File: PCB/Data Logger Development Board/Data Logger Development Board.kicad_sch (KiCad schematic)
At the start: 15 parts, among them J1 TFBS4711-TR1, U1 STM32C091FCP6, U2 TPS631000DRLR, U3 MCP2122T-E/SN

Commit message: Added ADC for reading battery voltage, added temp sensor, added GPS breakout board
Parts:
- removed C2: 22uF, symbol Device:C
- added C10, C7: 100nF, symbol Device:C
- added C8, C9: 20pF, symbol Device:C
- added Q1, Q2, Q3, Q4, Q5, Q6: 2N7002, Package_TO_SOT_SMD:SOT-23_Handsoldering, symbol Transistor_FET:2N7002
- added R10, R11, R13, R15, R18, R20: 1kR, symbol Device:R
- added R12, R14, R16, R17, R19, R5, R6: 100kR, symbol Device:R
- added R7: 15kR, symbol Device:R
- added R8, R9: 10kR, symbol Device:R
- added TH1: NTCG164BH103JT1, symbol Device:Thermistor
- added U4: M95P32-IXMNT/E, SO8N_4X5X1P27_STM, symbol M95P32-IXMNT/E:M95P32-IXMNT_E
- added U5: MCP7940N-I/MS, MSOP8_MC_MCH, symbol MCP7940N-I/MS:MCP7940N-I_MS
- added U6: 120591-1, CONN3_120591-1_TEC, symbol MP000357:120591-1
- added U7: VEML7700-TR, VEML7700-TR, symbol VEML7700-TR:VEML7700-TR
- added U8: ~, symbol M95P32-IXMNT/E:GY-NEO6MV2
- added Y1: 32.768kHz, symbol Device:Crystal
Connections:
- net 3.3V_REG: now also C10.2, C7.1, R6.2, TH1.1, U4.8 (VCC), U5.8 (VCC), U7.2 (VDD), U8.1 (VCC)
- net BAT_OUT: now also R8.1
- net GND: now also C10.1, C7.2, C8.2, C9.2, Q1.2 (S), Q2.2 (S), Q3.2 (S), Q4.2 (S), Q5.2 (S), Q6.2 (S), R12.1, R14.1, R16.1, R17.1, R19.1, R5.1, U4.1 (*S), U6.3 (GND), U8.4 (GND); no longer U3.4 (VSS)
- net I2C_SCL: now also U5.6 (SCL), U7.1 (SCL)
- net I2C_SDA: now also U5.5 (SDA), U7.4 (SDA)
- net MEMORY #WP: now also U4.3 (*W-DQ2)
- net SPI MOSI: now also U4.5 (D-DQ0)
- net SPI_CLK: now also U4.6 (C)
- net SPI_MISO: now also U1.16 (PA11[PA9]), U4.2 (Q-DQ1); no longer U1.13 (PA6)
- net USART1_TX: now also U1.2 (PC14-OSCX_IN); no longer U1.7 (PA0)
- net USART2_RX: now reaches U1.18 (PA13)
- net USART2_RX: now also U8.3 (TX)
- net USART2_TX: now reaches U1.19 (PA14-BOOT0/PA15)
- net USART2_TX: now also U8.2 (RX)
- net MEMORY CS renamed WAKEUP
- net WAKEUP: now also R10.1, R11.2, R13.1, R15.1, R18.1, R20.1
- new net: C9.1, U5.2 (X2), Y1.2
- new net: Q1.1 (G), R11.1, R5.2
- new net: Q1.3 (D), R9.2
- new net: U5.3 (VBAT), U6.1 (VBat), U6.2 (VBat)
- new net: Q6.1 (G), R19.2, R20.2
- new net: Q3.1 (G), R13.2, R14.2
- new net: Q6.3 (D), U3.4 (VSS)
- new net: Q5.1 (G), R17.2, R18.2
- new net: C8.1, U5.1 (X1), Y1.1
- new net: Q4.1 (G), R15.2, R16.2
- new net: Q3.3 (D), U5.4 (VSS)
- new net: R7.1, TH1.2, U1.13 (PA6)
- new net: Q4.3 (D), U7.3 (GND)
- new net: Q5.3 (D), U4.4 (VSS)
- new net: R6.1, U4.7 (*HOLD-DQ3)
- new net: Q2.1 (G), R10.2, R12.2
- new net: Q2.3 (D), R7.2
- new net BAT_ADC: R8.2, R9.1, U1.7 (PA0)
- no-connect marks 5 -> 2
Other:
- note added: "TO DO: ADD BATTERY CONNECTOR AND PROTECTION ADD PRESSURE SENSOR ADD OPTIONAL GPIO EXPANDER TO CONTROL POWER TO INDIVIDUAL SECTIONS"
- note removed: "TO DO: ADD EXTERNAL MEMORY ADD BATTERY CONNECTOR AND PROTECTION"
- moved on the sheet: C3, C4, R3, R4, U1

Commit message: revised sensor power control and started adding batteries and battery protection
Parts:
- removed Q2, Q3, Q4, Q5, Q6: 2N7002, Package_TO_SOT_SMD:SOT-23_Handsoldering, symbol Transistor_FET:2N7002
- removed R12, R16, R17, R19: 100kR, symbol Device:R
- removed R15, R18, R20: 1kR, symbol Device:R
- removed TH1: NTCG164BH103JT1, symbol Device:Thermistor
- added C2: 100nF, symbol Device:C
- added F1, F2, F3, F4: 1A Fuse, symbol Device:Fuse
- added Q3: AO3401A, Package_TO_SOT_SMD:SOT-23, symbol Transistor_FET:AO3401A
- added U10: AP9101CAK6-ANTRG1, AP9101CAK6-ANTRG1_DIO, symbol AP9101CAK6-ANTRG1:AP9101CAK6-ANTRG1
- added U9: ~, symbol AMDLA1004S-1R0MT:18650_4_Cell_Holder
- R10: value 1kR -> 2.7kR
- R13: value 1kR -> 10kR
- R14: value 100kR -> 100R
- R7: value 15kR -> 330R
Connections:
- net 3.3V_REG: now also R13.1, Q3.2 (S); no longer C10.2, C5.2, C6.2, C7.1, J1.1 (VCC_ANODE), J1.5 (VCC), R6.2, U3.8 (VDD), U4.8 (VCC), U5.8 (VCC), U7.2 (VDD)
- net GND: now also J1.4 (SHUTDOWN), U3.4 (VSS), U4.4 (VSS), U5.4 (VSS), U7.3 (GND); no longer R14.1
- net at R13.2: now also R14.1, Q3.1 (G); no longer R14.2
- net at U1.13 (PA6): no longer R7.1
- net at R7.2: now also C2.1, U10.5 (VDD)
- net LED_SHUTDOWN renamed 3.3V_ENABLE
- net 3.3V_ENABLE: now also R14.2; no longer J1.4 (SHUTDOWN)
- net WAKEUP renamed ADC_DIVIDER_ENABLE
- net ADC_DIVIDER_ENABLE: no longer R10.1, R13.1
- new net: F4.2, U9.4 (Cell4+)
- new net: F2.2, U9.2 (Cell2+)
- new net: F3.2, U9.3 (Cell3+)
- new net: F1.2, U9.1 (Cell1+)
- new net: R10.1, U10.2 (VM)
- new net 3.3V_SWITCHED: C10.2, C5.2, C6.2, C7.1, J1.1 (VCC_ANODE), J1.5 (VCC), Q3.3 (D), R6.2, U3.8 (VDD), U4.8 (VCC), U5.8 (VCC), U7.2 (VDD)
- new net BATT_PACK_+: F1.1, F2.1, F3.1, F4.1, R7.1
- new net BATT_PACK_-: C2.2, U10.6 (VSS), U9.5 (Cell4-), U9.6 (Cell3-), U9.7 (Cell2-), U9.8 (Cell1-)
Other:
- note added: "BATTERY CHARGING IC"
- note added: "BATTERY MOSFETS IRF7313TRPBFXTMA1"
- note added: "TO DO: ADD BATTERY PROTECTION AND CHARGING IC ADD PROGRAMMING HEADER GAS TEMP AND HUMIDITY SENSOR"
- note removed: "TO DO: ADD BATTERY CONNECTOR AND PROTECTION ADD PRESSURE SENSOR ADD OPTIONAL GPIO EXPANDER TO CONTROL POWER TO INDIVIDUAL SECTIONS"
- moved on the sheet: C1, C10, C5, C6, J1, L1, Q1, R1, R11, R2, R5, R6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

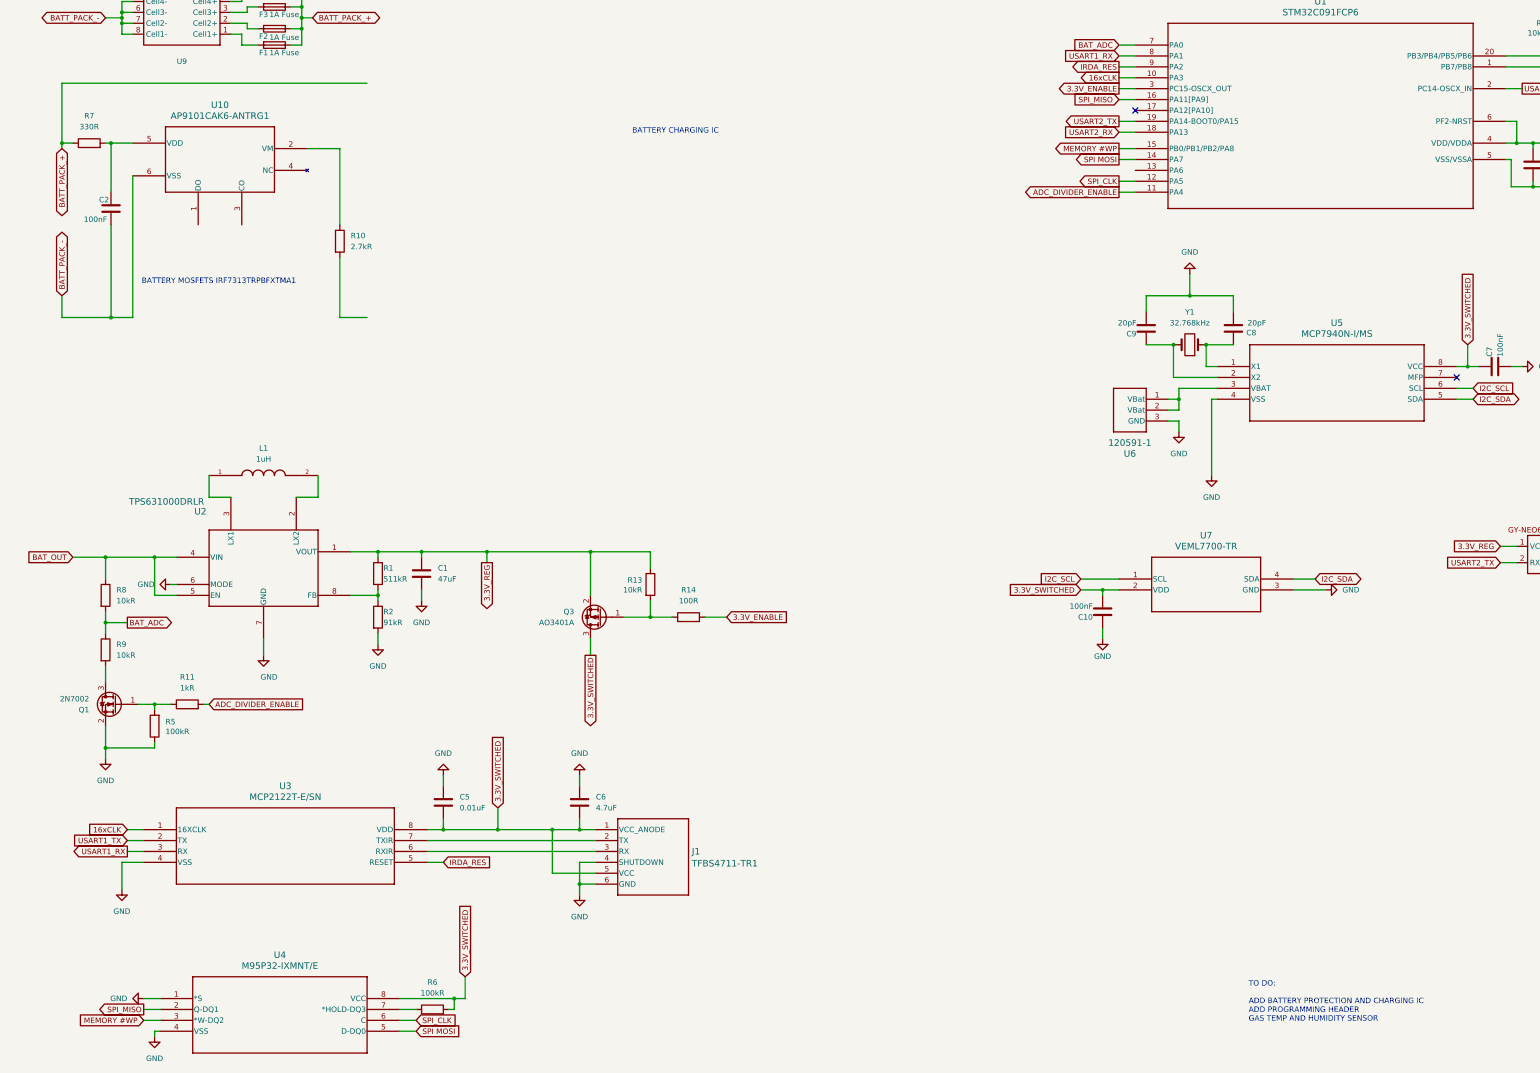
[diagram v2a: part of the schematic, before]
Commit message: added battery protection mosfets
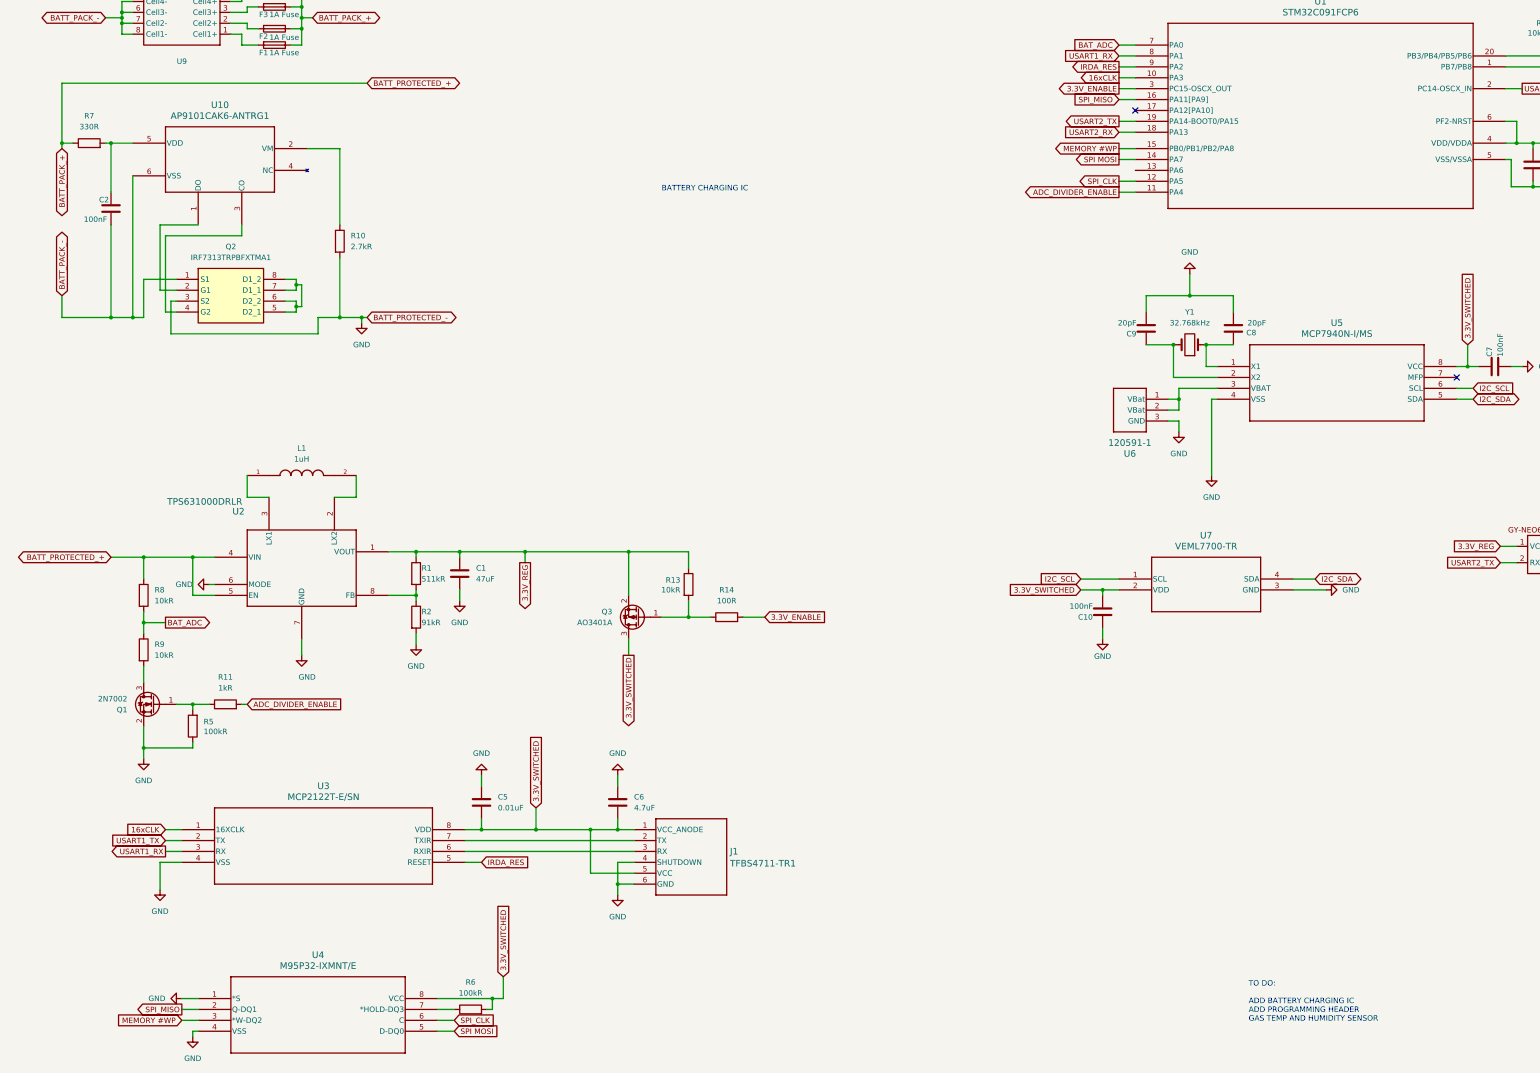
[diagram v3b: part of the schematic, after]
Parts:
- added Q2: IRF7313TRPBFXTMA1, SOIC127P600X175-8N, symbol IRF7313TRPBFXTMA1:IRF7313TRPBFXTMA1
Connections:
- net BAT_OUT is gone; now on net BATT_PACK_+: R8.1, U2.4 (VIN), U2.5 (EN)
- net BATT_PACK_-: now also Q2.1 (S1)
- net GND: now also R10.2, Q2.3 (S2)
- net at U10.1 (DO): now also Q2.2 (G1)
- net at U10.3 (CO): now also Q2.4 (G2)
- new net: Q2.5 (D2_1), Q2.6 (D2_2), Q2.7 (D1_1), Q2.8 (D1_2)
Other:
- note added: "TO DO: ADD BATTERY CHARGING IC ADD PROGRAMMING HEADER GAS TEMP AND HUMIDITY SENSOR"
- note removed: "BATTERY MOSFETS IRF7313TRPBFXTMA1"
- note removed: "TO DO: ADD BATTERY PROTECTION AND CHARGING IC ADD PROGRAMMING HEADER GAS TEMP AND HUMIDITY SENSOR"
- moved on the sheet: C1, C5, C6, J1, L1, Q1, Q3, R1, R11, R13, R14, R2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

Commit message: added charging solution
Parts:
- added C11, C12, C13, C14, C15: 22uF, symbol Device:C
- added L2: 1uH, AMDLA1004S-1R0MT:IND_AMDLA1004S-1R0MT, symbol AMDLA1004S-1R0MT:AMDLA1004S-1R0MT
- added R12: 0.5R, symbol Device:R
- added U11: IP5306_CK, IP5306:SOP127P600X165-9N, symbol IP5306:IP5306
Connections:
- net BATT_PACK_+: now also C12.1, L2.2, R12.1; no longer R8.1, U2.4 (VIN), U2.5 (EN)
- net GND: now also C11.2, C12.2, C13.2, C14.2, C15.2, U11.9 (POWERPAD)
- new net: C11.1, R12.2, U11.6 (BAT)
- new net: L2.1, U11.7 (SW)
- new net 5V: C13.1, C14.1, C15.1, R8.1, U11.8 (VOUT), U2.4 (VIN), U2.5 (EN)
- no-connect marks 2 -> 6
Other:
- note added: "TO DO: ADD PROGRAMMING HEADER GAS TEMP AND HUMIDITY SENSOR"
- note removed: "BATTERY CHARGING IC"
- note removed: "TO DO: ADD BATTERY CHARGING IC ADD PROGRAMMING HEADER GAS TEMP AND HUMIDITY SENSOR"
- moved on the sheet: C10, C2, C3, C4, C7, C8, C9, F1, F2, F3, F4, Q2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
